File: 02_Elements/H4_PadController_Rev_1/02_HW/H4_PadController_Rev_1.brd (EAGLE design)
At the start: 67 x 45 mm, 23 parts

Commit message: Implemented H4_PadController_Rev_1 Schematic
Added Provisional Mechanic LaserCuts for PADs.

Implemented all Schematic despite 8to1 4051 Multiplexer (tomorrow ^.^ )
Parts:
- removed C_ESP_3: 470pF, adafruit:C0805K
- removed D2, D3: MBRA140, SparkFun-DiscreteSemi:SMA-DIODE
- removed J_PW: (no value), SparkFun:JST-2-SMD
- removed R_ESP0, R_ESP1, R_ESP2, R_ESP3, R_ESP4: 12KOhm, adafruit:M0805
- removed SW_PW: TL36YO, switch:TL3XYO
- added C_DC_0, R_LED_0, R_LED_1, R_LED_2, R_LED_3, R_LED_4, R_LED_5, R_LED_6, R_LED_7: 10uF, adafruit:C1206
- added C_DC_1: 100nF, adafruit:C1206
- added J_AUX: (no value), adafruit:1X08-BIG
- added J_IN: 22-05-7048-04, con-molex:7395-04
- added J_LED: 22-05-7038-03, con-molex:7395-03
- added L_RGB_2, L_RGB_3, L_RGB_4, L_RGB_5, L_RGB_6, L_RGB_7: (no value), SparkFun-LED:WS2812B
- added R_ESP5, R_ESP6: 12KOhm, adafruit:M1206
- added R_I2C_0, R_I2C_1, R_SET_0, R_SET_1, R_SET_2: 10KOhm, adafruit:M1206
- added SW_FLASH, SW_RESET: (no value), switch-omron:B3F-10XX
- added U_MUX: 4051D, 40xx:SO16
- C_VR_0, C_VR_1, C_VR_2, C_VR_3: device adafruit:C0805 -> adafruit:C1206
- R_PW1: device adafruit:M0805 -> adafruit:M1206
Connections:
- removed net EN: R_ESP2.1
- removed net GPIO0: R_ESP0.1
- removed net GPIO15: R_ESP4.1
- removed net GPIO2: R_ESP1.1
- removed net LED_RGB: L_RGB_0.4
- removed net N$31: J_PW.2, SW_PW.2
- removed net N$36: SW_PW.3
- removed net NRST: C_ESP_3.1, R_ESP3.1
- removed net V33: C_VR_2.1, D3.C, U_VR_1.1
- removed net V5: C_VR_0.1, D2.C, U_VR_0.1
- new net FLASH: R_ESP6.2, SW_FLASH.3, X2.12
- new net GPIO12: J_AUX.4, X2.6
- new net GPIO13: J_AUX.3, X2.7
- new net GPIO16: J_AUX.5, X2.4
- new net I2C_SCL: J_AUX.1, R_I2C_0.1, X2.13
- new net I2C_SDA: J_AUX.2, R_I2C_1.1, X2.14
- new net LED: L_RGB_0.4, L_RGB_5.4, X2.5
- new net LED_OUT: J_LED.2, L_RGB_7.2
- new net N$1: U_MUX.13
- new net N$11: L_RGB_3.2
- new net N$12: U_MUX.15
- new net N$13: U_MUX.12
- new net N$14: L_RGB_4.4, L_RGB_5.2
- new net N$15: J_IN.2
- new net N$16: J_IN.3
- new net N$17: L_RGB_4.2, L_RGB_6.4
- new net N$18: R_SET_0.1, X2.11
- new net N$19: R_SET_1.1, X2.10
- new net N$2: R_SET_2.2, X2.3
- new net N$20: L_RGB_6.2, L_RGB_7.4
- new net N$21: U_MUX.1
- new net N$22: U_MUX.5
- new net N$23: U_MUX.2
- new net N$24: U_MUX.4
- new net N$25: U_MUX.6
- new net N$26: U_MUX.11
- new net N$27: U_MUX.10
- new net N$28: U_MUX.9
- new net N$29: U_MUX.3
- new net N$3: L_RGB_2.2, L_RGB_3.4
- new net N$4: X2.16
- new net N$6: U_MUX.14
- new net N$7: X2.15
- new net PAD: X2.2
- new net RST: R_ESP5.2, SW_RESET.3, X2.1
- new net VEE: U_MUX.7
- net 3V3: now also C_DC_0.1, C_DC_1.1, J_AUX.7, R_ESP5.1, R_ESP6.1, R_I2C_0.2, R_I2C_1.2, R_SET_0.2, R_SET_2.1, X2.8; no longer R_ESP0.2, R_ESP2.2, R_ESP3.2
- net 5V: now also J_AUX.8, J_LED.3, L_RGB_2.1, L_RGB_3.1, L_RGB_4.1, L_RGB_5.1, L_RGB_6.1, L_RGB_7.1, R_LED_0.1, R_LED_1.1, R_LED_2.1, R_LED_3.1, R_LED_4.1, R_LED_5.1, R_LED_6.1, R_LED_7.1
- net GND: now also C_DC_0.2, C_DC_1.2, J_AUX.6, J_IN.1, J_LED.1, L_RGB_2.3, L_RGB_3.3, L_RGB_4.3, L_RGB_5.3, L_RGB_6.3, L_RGB_7.3, R_LED_0.2, R_LED_1.2, R_LED_2.2, R_LED_3.2, R_LED_4.2, R_LED_5.2, R_LED_6.2, R_LED_7.2, R_SET_1.2, SW_FLASH.1, SW_RESET.1, U_MUX.8; no longer C_ESP_3.2, J_PW.1, R_ESP1.2, R_ESP4.2
- net N$9: now also L_RGB_2.4
- net VCC: now also U_MUX.16; no longer X2.8
- net VIN: now also C_VR_0.1, C_VR_2.1, J_IN.4, U_VR_0.1, U_VR_1.1; no longer D2.A, D3.A, SW_PW.1
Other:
- board outline removed

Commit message: Finished H4_PadController_Rev_1 Schematic
The Schematic has been finished! Yay!
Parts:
- added C_MUX: 10uF, adafruit:C1206
- added J_PAD: 22-27-2101-10, con-molex:6410-10
- added J_PRG: 22-27-2051-05, con-molex:6410-05
- added R_BRIDGE: 220Ohm, adafruit:M1206
- added R_PAD_0, R_PAD_1: 0Ohm, adafruit:M1206
- moved U_MUX 250.0 mm to (-10.0, 34.0), turned to 90 degrees
- moved J_LED 188.3 mm to (57.0, 8.00), flipped to the bottom, turned to 270 degrees
- moved J_IN 133.8 mm to (14.0, 8.00), flipped to the bottom, turned to 90 degrees
- moved X2 22.8 mm to (32.0, 8.00), flipped to the bottom, turned to 270 degrees
- moved U_VR_0 4.00 mm to (18.0, 31.0), flipped to the bottom
- flipped U_VR_1 to the bottom
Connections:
- removed net GPIO16: J_AUX.5, X2.4
- removed net N$1: U_MUX.13
- removed net N$12: U_MUX.15
- removed net N$13: U_MUX.12
- removed net N$21: U_MUX.1
- removed net N$22: U_MUX.5
- removed net N$23: U_MUX.2
- removed net N$24: U_MUX.4
- removed net N$25: U_MUX.6
- removed net N$26: U_MUX.11
- removed net N$27: U_MUX.10
- removed net N$28: U_MUX.9
- removed net N$29: U_MUX.3
- removed net N$4: X2.16
- removed net N$6: U_MUX.14
- removed net N$7: X2.15
- removed net VCC: U_MUX.16
- removed net VEE: U_MUX.7
- new net MUX_A: J_AUX.5, U_MUX.11, X2.4
- new net MUX_B: U_MUX.10, X2.6
- new net MUX_C: U_MUX.9, X2.7
- new net PAD_0: J_PAD.8, U_MUX.13
- new net PAD_1: J_PAD.7, U_MUX.14
- new net PAD_2: J_PAD.6, U_MUX.15
- new net PAD_3: J_PAD.5, U_MUX.12
- new net PAD_4: J_PAD.4, U_MUX.1
- new net PAD_5: J_PAD.3, U_MUX.5
- new net PAD_6: J_PAD.2, U_MUX.2
- new net PAD_7: J_PAD.1, U_MUX.4
- new net PAD_MUX: R_PAD_0.1, U_MUX.3
- new net PAD_SINGLE: J_PAD.9, R_PAD_1.1
- new net RX: J_PRG.4, X2.15
- new net TX: J_PRG.3, X2.16
- net 3V3: now also C_MUX.1, J_PRG.5, R_BRIDGE.1, U_MUX.16, U_MUX.6, U_MUX.7
- net 5V: now also J_PRG.1
- net GND: now also C_MUX.2, J_PAD.10, J_PRG.2
- net GPIO12: no longer X2.6
- net GPIO13: no longer X2.7
- net PAD: now also R_BRIDGE.2, R_PAD_0.2, R_PAD_1.2

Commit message: Finished Routing H4_PadController_Rev_1
Finished the Routing of the full Element H4_PadController_Rev_4.

Need to make Silk, 3D model, Gerber Files and BOM.
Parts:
- removed C_DC_0, C_MUX, R_LED_0, R_LED_1, R_LED_2, R_LED_3, R_LED_4, R_LED_5, R_LED_6, R_LED_7: 10uF, adafruit:C1206
- removed C_DC_1, C_VR_3: 100nF, adafruit:C1206
- removed C_VR_2: 330nF, adafruit:C1206
- removed J_AUX: (no value), adafruit:1X08-BIG
- removed J_IN: 22-05-7048-04, con-molex:7395-04
- removed J_LED: 22-05-7038-03, con-molex:7395-03
- removed J_PAD: 22-27-2101-10, con-molex:6410-10
- removed J_PRG: 22-27-2051-05, con-molex:6410-05
- removed LED_PW, LED_PW1: (no value), adafruit:1206
- removed L_RGB_6, L_RGB_7: (no value), SparkFun-LED:WS2812B
- removed R_BRIDGE: 220Ohm, adafruit:M1206
- removed R_ESP5, R_ESP6: 12KOhm, adafruit:M1206
- removed R_PAD_0, R_PAD_1: 0Ohm, adafruit:M1206
- removed R_PW, R_PW1: 330Ohm, adafruit:M1206
- removed R_SET_0, R_SET_1, R_SET_2: 10KOhm, adafruit:M1206
- removed SW_FLASH, SW_RESET: (no value), switch-omron:B3F-10XX
- removed U_MUX: 4051D, 40xx:SO16
- removed U_VR_1: UA78M33DCY, linear:SOT223
- removed X2: (no value), adafruit:ESP-12
- added C_ATM_0, C_ATM_1, C_ATM_2: 0.1uF, adafruit:C0805
- added C_LED: 100uF, adafruit:C1210
- added D_RST: (no value), microbuilder:SOD-123
- added J_CON_00, J_CON_01, J_CON_02, J_CON_03: (no value), SparkFun-Connectors:1X02_2.54_SCREWTERM
- added R_LED: 47Ohm, adafruit:M0805
- added R_PAD_00, R_PAD_01, R_PAD_02, R_PAD_03: 220Ohm, adafruit:M0805
- added R_RST: 10kOhm, adafruit:M0805
- added SV1: (no value), con-lstb:MA06-1
- added U_ATMEGA328: ATMEGA328P_TQFP, SparkFun-DigitalIC:TQFP32-08
- added U_OSC: ABM8-24.000MHZ-B2-T, ABM8-24.000MHZ-B2-T:OSCSC320X250X100N
- added U_PAD_0, U_PAD_1, U_PAD_2, U_PAD_3, U_PAD_GND: PAD_CONNECTOR_MULTI, atfHenar_customLib:PAD_CONNECTOR_MULTI
- C_VR_0, C_VR_1: device adafruit:C1206 -> adafruit:C0805
- R_I2C_0, R_I2C_1: value 10KOhm -> 10kOhm; device adafruit:M1206 -> adafruit:M0805
- moved L_RGB_5 243.3 mm to (57.5, 7.50), turned to 180 degrees
- moved L_RGB_4 232.7 mm to (48.5, 7.50), turned to 180 degrees
- moved L_RGB_3 213.5 mm to (39.5, 7.50), turned to 180 degrees
- moved R_I2C_1 205.4 mm to (62.0, 7.50), flipped to the bottom, turned to 90 degrees
- moved R_I2C_0 203.8 mm to (62.0, 11.5), flipped to the bottom, turned to 270 degrees
- moved L_RGB_2 198.7 mm to (30.5, 7.50), turned to 180 degrees
- moved C_VR_1 112.1 mm to (58.5, 7.50), flipped to the bottom, turned to 90 degrees
- moved C_VR_0 80.8 mm to (58.5, 11.5), flipped to the bottom, turned to 270 degrees
- moved L_RGB_0 53.1 mm to (12.5, 7.50), turned to 180 degrees
- moved L_RGB_1 40.7 mm to (21.5, 7.50), turned to 180 degrees
- moved U_VR_0 36.9 mm to (48.0, 9.50), turned to 270 degrees
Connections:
- removed net 3V3: C_DC_0.1, C_DC_1.1, C_MUX.1, C_VR_3.1, J_AUX.7, J_PRG.5, R_BRIDGE.1, R_ESP5.1, R_ESP6.1, R_I2C_0.2, R_I2C_1.2, R_PW1.2, R_SET_0.2, R_SET_2.1, U_MUX.16, U_MUX.6, U_MUX.7, U_VR_1.3, X2.8
- removed net FLASH: R_ESP6.2, SW_FLASH.3, X2.12
- removed net GPIO12: J_AUX.4
- removed net GPIO13: J_AUX.3
- removed net MUX_A: J_AUX.5, U_MUX.11, X2.4
- removed net MUX_B: U_MUX.10, X2.6
- removed net MUX_C: U_MUX.9, X2.7
- removed net N$11: L_RGB_3.2
- removed net N$15: J_IN.2
- removed net PAD: R_BRIDGE.2, R_PAD_0.2, R_PAD_1.2, X2.2
- removed net PAD_0: J_PAD.8, U_MUX.13
- removed net PAD_1: J_PAD.7, U_MUX.14
- removed net PAD_2: J_PAD.6, U_MUX.15
- removed net PAD_3: J_PAD.5, U_MUX.12
- removed net PAD_4: J_PAD.4, U_MUX.1
- removed net PAD_5: J_PAD.3, U_MUX.5
- removed net PAD_6: J_PAD.2, U_MUX.2
- removed net PAD_7: J_PAD.1, U_MUX.4
- removed net PAD_MUX: R_PAD_0.1, U_MUX.3
- removed net PAD_SINGLE: J_PAD.9, R_PAD_1.1
- removed net RX: J_PRG.4, X2.15
- removed net TX: J_PRG.3, X2.16
- new net ADC_OUT: U_ATMEGA328.19
- new net LEDE: L_RGB_3.2, L_RGB_4.4
- new net MISO: SV1.6, U_ATMEGA328.16
- new net MOSI: SV1.5, U_ATMEGA328.15
- new net N$1: U_ATMEGA328.30
- new net N$13: U_ATMEGA328.22
- new net N$21: U_ATMEGA328.12
- new net N$22: U_ATMEGA328.13
- new net N$23: U_ATMEGA328.14
- new net N$4: C_ATM_2.1, U_ATMEGA328.20
- new net N$6: U_ATMEGA328.31
- new net PAD_00: R_PAD_00.2, U_ATMEGA328.23, U_PAD_0.P$1
- new net PAD_01: R_PAD_01.2, U_ATMEGA328.24, U_PAD_1.P$1
- new net PAD_02: R_PAD_02.2, U_ATMEGA328.25, U_PAD_2.P$1
- new net PAD_03: R_PAD_03.2, U_ATMEGA328.26, U_PAD_3.P$1
- new net SCK: SV1.4, U_ATMEGA328.17
- net 5V: now also C_ATM_0.1, C_ATM_1.1, C_LED.1, D_RST.C, R_I2C_0.2, R_I2C_1.2, R_PAD_00.1, R_PAD_01.1, R_PAD_02.1, R_PAD_03.1, R_RST.1, SV1.2, U_ATMEGA328.18, U_ATMEGA328.4, U_ATMEGA328.6; no longer J_AUX.8, J_LED.3, J_PRG.1, L_RGB_6.1, L_RGB_7.1, R_LED_0.1, R_LED_1.1, R_LED_2.1, R_LED_3.1, R_LED_4.1, R_LED_5.1, R_LED_6.1, R_LED_7.1, R_PW.2
- net GND: now also C_ATM_0.2, C_ATM_1.2, C_ATM_2.2, C_LED.2, J_CON_01.P1, J_CON_03.P1, SV1.1, U_ATMEGA328.21, U_ATMEGA328.3, U_ATMEGA328.5, U_OSC.2, U_OSC.4, U_PAD_GND.P$1; no longer C_DC_0.2, C_DC_1.2, C_MUX.2, C_VR_2.2, C_VR_3.2, J_AUX.6, J_IN.1, J_LED.1, J_PAD.10, J_PRG.2, LED_PW.C, LED_PW1.C, L_RGB_6.3, L_RGB_7.3, R_LED_0.2, R_LED_1.2, R_LED_2.2, R_LED_3.2, R_LED_4.2, R_LED_5.2, R_LED_6.2, R_LED_7.2, R_SET_1.2, SW_FLASH.1, SW_RESET.1, U_MUX.8, U_VR_1.2, U_VR_1.4, X2.9
- net I2C_SCL: now also J_CON_01.P2, J_CON_03.P2, R_I2C_1.1, U_ATMEGA328.28; no longer J_AUX.1, R_I2C_0.1, X2.13
- net I2C_SDA: now also J_CON_00.P1, J_CON_02.P1, R_I2C_0.1, U_ATMEGA328.27; no longer J_AUX.2, R_I2C_1.1, X2.14
- net LED: now also R_LED.2; no longer L_RGB_5.4, X2.5
- net LED_OUT: now also L_RGB_5.2; no longer J_LED.2, L_RGB_7.2
- net N$14: now also L_RGB_4.2, L_RGB_5.4; no longer L_RGB_4.4, L_RGB_5.2
- net N$16: now also U_ATMEGA328.1; no longer J_IN.3
- net N$17: now also U_ATMEGA328.2; no longer L_RGB_4.2, L_RGB_6.4
- net N$18: now also U_ATMEGA328.9; no longer R_SET_0.1, X2.11
- net N$19: now also U_ATMEGA328.10; no longer R_SET_1.1, X2.10
- net N$2: now also U_ATMEGA328.7, U_OSC.3; no longer R_SET_2.2, X2.3
- net N$20: now also U_ATMEGA328.11; no longer L_RGB_6.2, L_RGB_7.4
- net N$5: now also U_ATMEGA328.8, U_OSC.1; no longer LED_PW.A, R_PW.1
- net N$8: now also R_LED.1, U_ATMEGA328.32; no longer LED_PW1.A, R_PW1.1
- net RST: now also D_RST.A, R_RST.2, SV1.3, U_ATMEGA328.29; no longer R_ESP5.2, SW_RESET.3, X2.1
- net VIN: now also J_CON_00.P2, J_CON_02.P2; no longer C_VR_2.1, J_IN.4, U_VR_1.1
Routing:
- net 5V: track 0.00 -> 129.9 mm, vias 0 -> 9
- net GND: track 0.00 -> 126.7 mm, vias 0 -> 7
- net I2C_SDA: track 0.00 -> 117.8 mm, vias 0 -> 1
- net I2C_SCL: track 0.00 -> 113.6 mm, vias 0 -> 4
- net VIN: track 0.00 -> 75.0 mm, vias 0 -> 1
- net PAD_00: track 0.00 -> 39.6 mm, vias 0 -> 2
- net PAD_01: track 0.00 -> 37.2 mm, vias 0 -> 2
- net RST: track 0.00 -> 29.8 mm, vias 0 -> 2
- net N$8: track 0.00 -> 25.9 mm, vias 0 -> 1
- net PAD_02: track 0.00 -> 20.0 mm, vias 0 -> 2
- net PAD_03: track 0.00 -> 17.4 mm, vias 0 -> 2
- net N$4: track 0.00 -> 14.8 mm, vias 0 -> 2
- net SCK: track 0.00 -> 10.7 mm, vias 0 -> 1
- net MOSI: track 0.00 -> 5.91 mm
- net N$3: track 0.00 -> 5.17 mm
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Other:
- board outline added: 70 x 17 mm

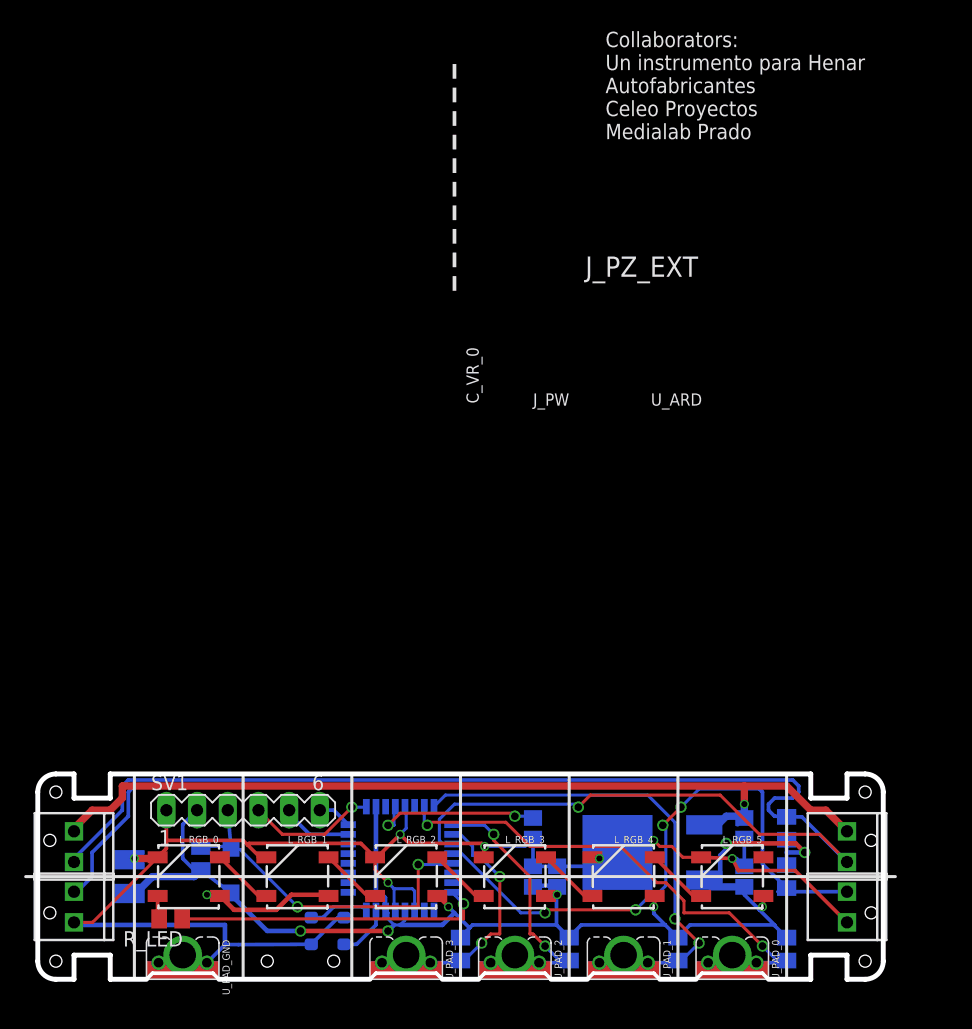
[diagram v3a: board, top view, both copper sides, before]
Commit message: H4_PadController_Rev_1 Finished Layout, Gerber Files and 3D Model
The PCB has been finished and the Layout, Gerber Files and 3D Model Finished.

TODO:
Make a better Schematic
Make a good BOM
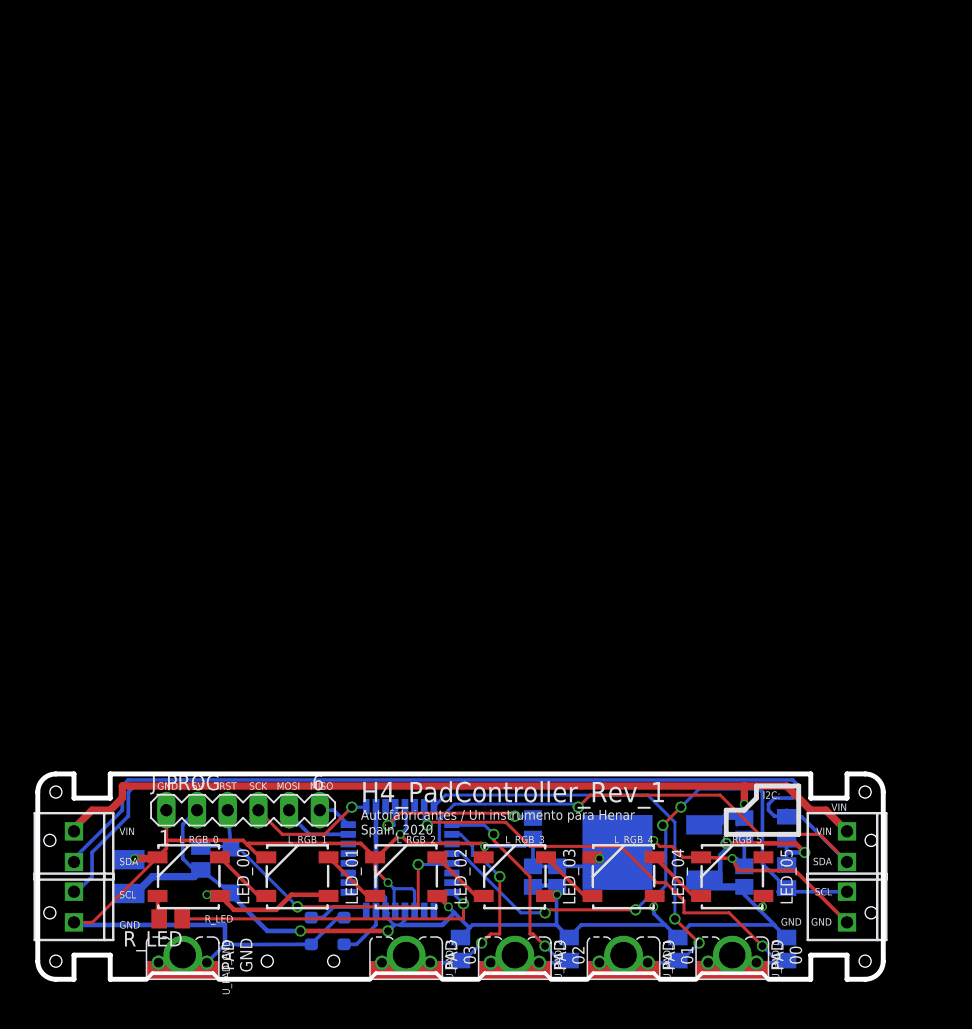
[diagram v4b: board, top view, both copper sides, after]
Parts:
- renumbered SV1 to J_PROG
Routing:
- added copper zone on layer 16, net FILLBOT
- added copper zone on layer 1, net FILLTOP
- added copper zone on layer 1, net GND
- added copper zone on layer 16, net GND
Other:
- board text added: "5V"
- board text added: "Autofabricantes / Un instrumento para Henar Spain, 2020"
- board text added: "C_ATM_0"
- board text added: "C_ATM_1"
- board text added: "C_ATM_2"
- board text added: "C_LED"
- board text added: "C_VR_1"
- board text added: "D_RST"
- board text added: "GND"
- board text added: "H4_PadController_Rev_1"
- board text added: "I2C:"
- board text added: "JCON_00/01"
- board text added: "J_CON_02/03"
- board text added: "J_PROG"
- board text added: "LED_00"
- board text added: "LED_01"
- board text added: "LED_02"
- board text added: "LED_03"
- board text added: "LED_04"
- board text added: "LED_05"
- board text added: "Licensed CC BY-SA 3.0"
- board text added: "MISO"
- board text added: "MOSI"
- board text added: "PAD 00"
- board text added: "PAD 01"
- board text added: "PAD 02"
- board text added: "PAD 03"
- board text added: "PAD GND"
- board text added: "RST"
- board text added: "R_I2C_0"
- board text added: "R_I2C_1"
- board text added: "R_LED"
- board text added: "R_PAD_00"
- board text added: "R_PAD_01"
- board text added: "R_PAD_02"
- board text added: "R_PAD_03"
- board text added: "R_RST"
- board text added: "SCK"
- board text added: "SCL"
- board text added: "SDA"
- board text added: "U_ATMEGA328"
- board text added: "U_OSC"
- board text added: "U_VR"
- board text added: "VIN"
- board text removed: "Collaborators: Un instrumento para Henar Autofabricantes Celeo Proyectos Medialab Prado"
- board text removed: "J_PW"
- board text removed: "J_PZ_EXT"
- board text removed: "R_LEDSTR"
- board text removed: "TX RX RST(NC) GND LED_STR MUX_A MUX_B MUX_C MUX_D LED_R LED_G LED_B"
- board text removed: "U_ARD"
